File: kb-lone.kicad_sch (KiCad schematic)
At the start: 464 parts, among them J1 TYPE-C-31-M12, J2 SM04B-SRSS-TB(LF)(SN), J3 SM04B-SRSS-TB(LF)(SN), J4 SSD1306, M1 RGB DB notch, Q1 DTC123JKAT146, SW1 K2-1187SQ-A4SW-06, SW10 F8, SW11 F9, SW12 F10, SW13 F11, SW14 F12, SW15 KNOB, SW16 GRV, SW17 1, SW18 2, SW19 3, SW2 ESC, SW20 4, SW21 5, SW22 6, SW23 7, SW24 8, SW25 9, SW26 0, SW27 MINUS, SW28 EQUAL, SW29 BSPC, SW3 F1, SW30 N/A, SW31 TAB, SW32 Q, SW33 W, SW34 E, SW35 R, SW36 T, SW37 Y, SW38 U, SW39 I, SW4 F2, SW40 O, SW41 P, SW42 LBRKT, SW43 RBRKT, SW44 BSLS, SW45 N/A, SW46 CAPS, SW47 A, SW48 S, SW49 D, SW5 F3, SW50 F, SW51 G, SW52 H, SW53 J, SW54 K, SW55 L, SW56 COLON, SW57 QUOTE, SW58 ENTER, SW59 PGUP, SW6 F4, SW60 LSHFT, SW61 Z, SW62 X, SW63 C, SW64 V, SW65 B, SW66 N, SW67 M, SW68 COMMA, SW69 DOT, SW7 F5, SW70 SLSH, SW71 RSHFT, SW72 UP, SW73 PGDN, SW74 LCTRL, SW75 WIN, SW76 LALT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

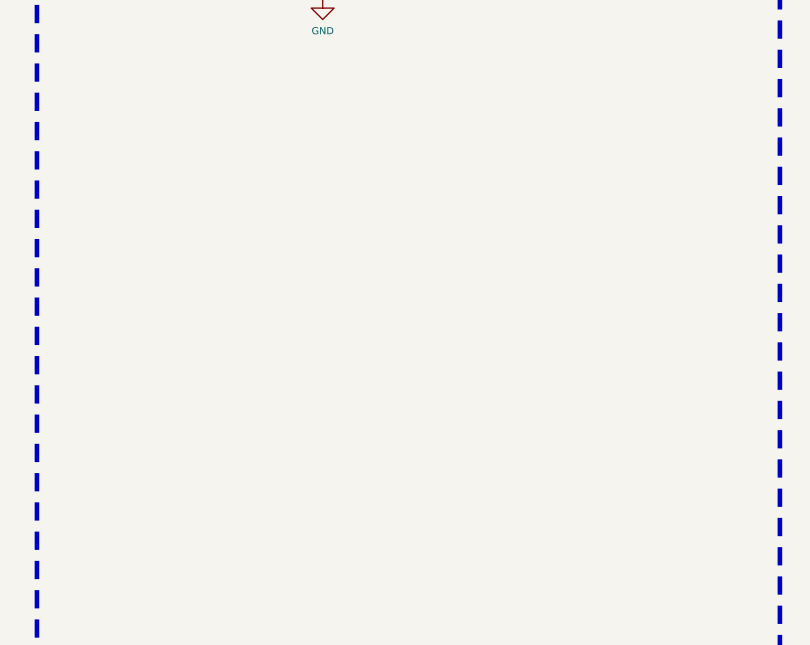
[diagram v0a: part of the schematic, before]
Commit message: add mounting holes
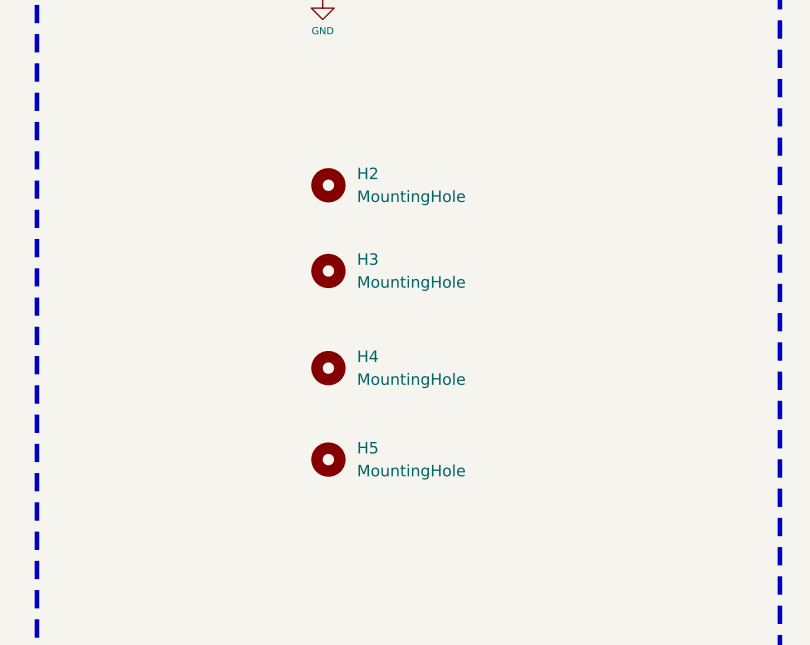
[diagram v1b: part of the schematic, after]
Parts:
- added H2, H3, H4, H5: MountingHole, acheron_Hardware:9774030243R, symbol Mechanical:MountingHole
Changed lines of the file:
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@@
     (pin "1")
   )
+  (symbol (lib_id "Mechanical:MountingHole") (at 280.035 93.98 0) (unit 1)
+    (in_bom yes) (on_board yes) (fields_autoplaced)
+    (property "Reference" "H3" (id 0) (at 283.21 92.7099 0)
+      (effects (font (size 1.27 1.27)) (justify left))
+    )
+    (property "Value" "MountingHole" (id 1) (at 283.21 95.2499 0)
+      (effects (font (size 1.27 1.27)) (justify left))
+    )
+    (property "Footprint" "acheron_Hardware:9774030243R" (id 2) (at 280.035 93.98 0)
+      (effects (font (size 1.27 1.27)) hide)
+    )
+    (property "Datasheet" "~" (id 3) (at 280.035 93.98 0)
+      (effects (font (size 1.27 1.27)) hide)
+    )
+  )
   (symbol (lib_id "acheron_Symbols:SK6812MINI-E") (at 745.49 525.145 0) (mirror y) (unit 1)
     (in_bom yes) (on_board yes)
@@
     (pin "2")
   )
+  (symbol (lib_id "Mechanical:MountingHole") (at 280.035 114.935 0) (unit 1)
+    (in_bom yes) (on_board yes) (fields_autoplaced)
+    (property "Reference" "H5" (id 0) (at 283.21 113.6649 0)
+      (effects (font (size 1.27 1.27)) (justify left))
+    )
+    (property "Value" "MountingHole" (id 1) (at 283.21 116.2049 0)
+      (effects (font (size 1.27 1.27)) (justify left))
+    )
+    (property "Footprint" "acheron_Hardware:9774030243R" (id 2) (at 280.035 114.935 0)
+      (effects (font (size 1.27 1.27)) hide)
+    )
+    (property "Datasheet" "~" (id 3) (at 280.035 114.935 0)
+      (effects (font (size 1.27 1.27)) hide)
+    )
+  )
   (symbol (lib_id "Device:C_Small") (at 352.425 729.615 90) (mirror x) (unit 1)
     (in_bom yes) (on_board yes)
@@
     (pin "4")
   )
+  (symbol (lib_id "Mechanical:MountingHole") (at 280.035 84.455 0) (unit 1)
+    (in_bom yes) (on_board yes) (fields_autoplaced)
+    (property "Reference" "H2" (id 0) (at 283.21 83.1849 0)
+      (effects (font (size 1.27 1.27)) (justify left))
+    )
+    (property "Value" "MountingHole" (id 1) (at 283.21 85.7249 0)
+      (effects (font (size 1.27 1.27)) (justify left))
+    )
+    (property "Footprint" "acheron_Hardware:9774030243R" (id 2) (at 280.035 84.455 0)
+      (effects (font (size 1.27 1.27)) hide)
+    )
+    (property "Datasheet" "~" (id 3) (at 280.035 84.455 0)
+      (effects (font (size 1.27 1.27)) hide)
+    )
+  )
   (symbol (lib_id "Device:R_Small") (at 789.94 775.335 180) (unit 1)
     (in_bom yes) (on_board yes)
@@
     (pin "2")
   )
+  (symbol (lib_id "Mechanical:MountingHole") (at 280.035 104.775 0) (unit 1)
+    (in_bom yes) (on_board yes) (fields_autoplaced)
+    (property "Reference" "H4" (id 0) (at 283.21 103.5049 0)
+      (effects (font (size 1.27 1.27)) (justify left))
+    )
+    (property "Value" "MountingHole" (id 1) (at 283.21 106.0449 0)
+      (effects (font (size 1.27 1.27)) (justify left))
+    )
+    (property "Footprint" "acheron_Hardware:9774030243R" (id 2) (at 280.035 104.775 0)
+      (effects (font (size 1.27 1.27)) hide)
+    )
+    (property "Datasheet" "~" (id 3) (at 280.035 104.775 0)
+      (effects (font (size 1.27 1.27)) hide)
+    )
+  )
   (symbol (lib_id "acheronSymbols:Mechanical_Switch") (at 287.02 287.02 0) (unit 1)
     (in_bom yes) (on_board yes)
@@
       (reference "H1") (unit 1) (value "9774035243R") (footprint "acheron_Hardware:9774035243R")
     )
+    (path "/ec6a840e-f49f-4977-8873-c61a354033f4"
+      (reference "H2") (unit 1) (value "MountingHole") (footprint "acheron_Hardware:9774030243R")
+    )
+    (path "/373bda51-d547-4a47-8abf-3dc83556bfa5"
+      (reference "H3") (unit 1) (value "MountingHole") (footprint "acheron_Hardware:9774030243R")
+    )
+    (path "/f6b76160-40ca-4e5a-a64f-e9aebc83cade"
+      (reference "H4") (unit 1) (value "MountingHole") (footprint "acheron_Hardware:9774030243R")
+    )
+    (path "/b4605cfc-6193-47bf-abd3-f9848adb9995"
+      (reference "H5") (unit 1) (value "MountingHole") (footprint "acheron_Hardware:9774030243R")
+    )
     (path "/888b62b0-e6e7-4413-9ebe-4d84f3056674"
